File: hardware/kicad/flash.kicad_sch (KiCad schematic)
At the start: 11 parts, among them U1 LFE5U-25F-6BG381C, U10 IS25LP128F-JBLE

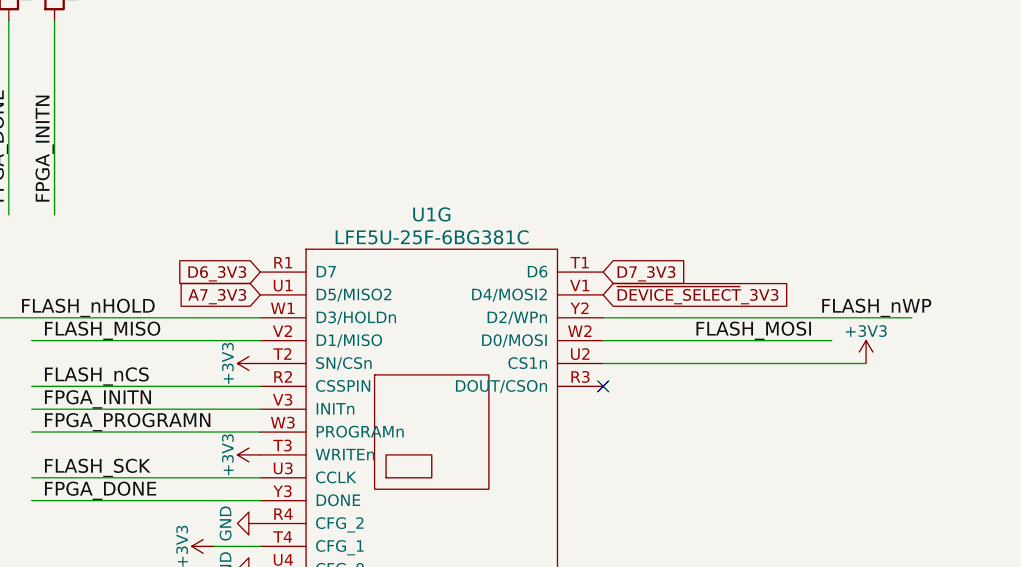
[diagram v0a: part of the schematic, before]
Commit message: Updated Rev. 1.1
- Wired Level Shifters
- Expansion GPIOs
- Oscillator
- Flash
- USB
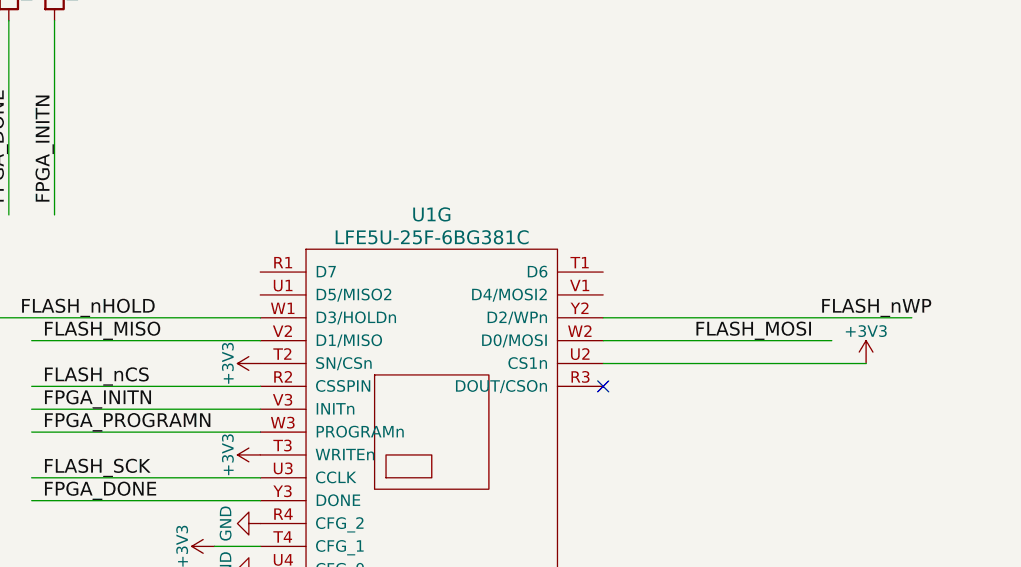
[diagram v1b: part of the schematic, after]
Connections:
- net A7_3V3: no longer names the net of U1.U1 (D5/MISO2)
- net D6_3V3: no longer names the net of U1.R1 (D7)
- net D7_3V3: no longer names the net of U1.T1 (D6)
- net ~{DEVICE_SELECT}_3V3: no longer names the net of U1.V1 (D4/MOSI2)
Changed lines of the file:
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@@
-		)
-	)
-	(global_label "D7_3V3"
-		(shape input)
-		(at 220.98 95.25 0)
-		(effects
-			(font
-				(size 1.27 1.27)
-			)
-			(justify left)
-		)
-		(property "Intersheetrefs" "${INTERSHEET_REFS}"
-			(at 220.98 95.25 90)
-			(effects
-				(font
-					(size 1.27 1.27)
-				)
-				(hide yes)
-			)
-		)
-	)
-	(global_label "A7_3V3"
-		(shape input)
-		(at 182.88 97.79 180)
-		(effects
-			(font
-				(size 1.27 1.27)
-			)
-			(justify right)
-		)
-		(property "Intersheetrefs" "${INTERSHEET_REFS}"
-			(at 182.88 97.79 90)
-			(effects
-				(font
-					(size 1.27 1.27)
-				)
-				(hide yes)
-			)
-		)
-	)
-	(global_label "~{DEVICE_SELECT}_3V3"
-		(shape input)
-		(at 220.98 97.79 0)
-		(effects
-			(font
-				(size 1.27 1.27)
-			)
-			(justify left)
-		)
-		(property "Intersheetrefs" "${INTERSHEET_REFS}"
-			(at 220.98 97.79 90)
-			(effects
-				(font
-					(size 1.27 1.27)
-				)
-				(hide yes)
-			)
-		)
-	)
-	(global_label "D6_3V3"
-		(shape input)
-		(at 182.88 95.25 180)
-		(effects
-			(font
-				(size 1.27 1.27)
-			)
-			(justify right)
-		)
-		(property "Intersheetrefs" "${INTERSHEET_REFS}"
-			(at 182.88 95.25 90)
-			(effects
-				(font
-					(size 1.27 1.27)
-				)
-				(hide yes)
-			)
 		)
 	)

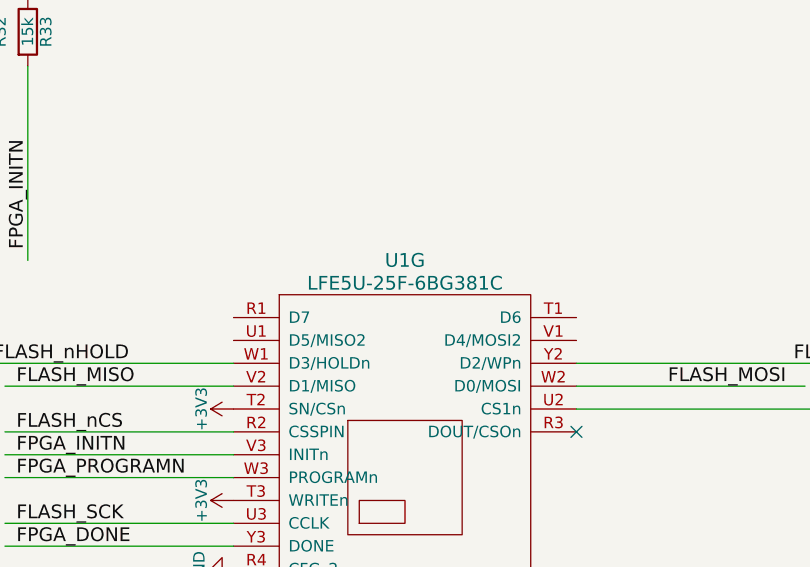
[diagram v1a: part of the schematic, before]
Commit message: Updates FPGA model in BOM and schematics
Replaces LFE5U-25F-6BG381C with LFE5U-85F-8BG381I in multiple files.
Ensures consistency across BOM, schematics, and PCB layouts for the updated FPGA model.
Adjusts related properties such as part number and connectivity attributes.

Addresses a hardware specification upgrade in branch 1.1.
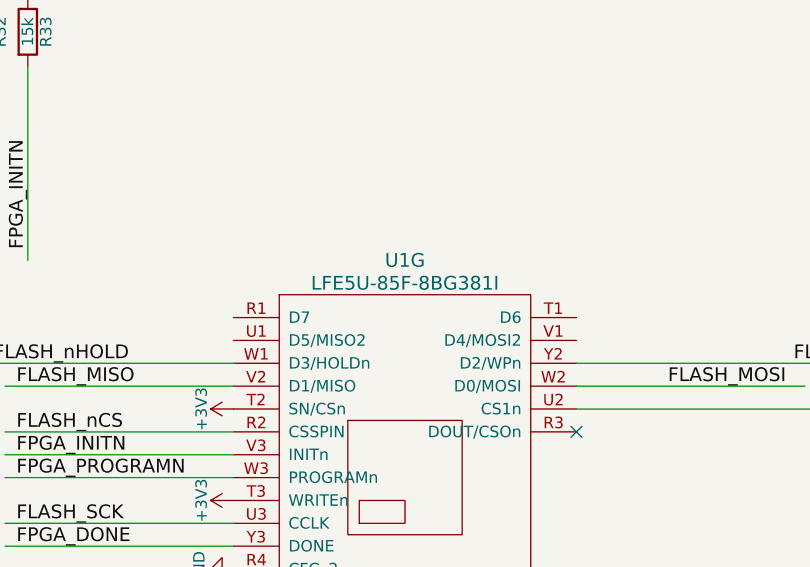
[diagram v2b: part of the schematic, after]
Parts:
- U1: value LFE5U-25F-6BG381C -> LFE5U-85F-8BG381I; MPN LFE5U-85F-6BG381C -> LFE5U-85F-8BG381I
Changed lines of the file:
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@@
 			)
 		)
-		(property "Value" "LFE5U-25F-6BG381C"
+		(property "Value" "LFE5U-85F-8BG381I"
 			(at 201.93 91.44 0)
 			(effects
@@
 			)
 		)
-		(property "MPN" "LFE5U-85F-6BG381C"
+		(property "MPN" "LFE5U-85F-8BG381I"
 			(at 201.93 113.03 0)
 			(effects
